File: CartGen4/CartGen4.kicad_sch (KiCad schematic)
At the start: 0 parts

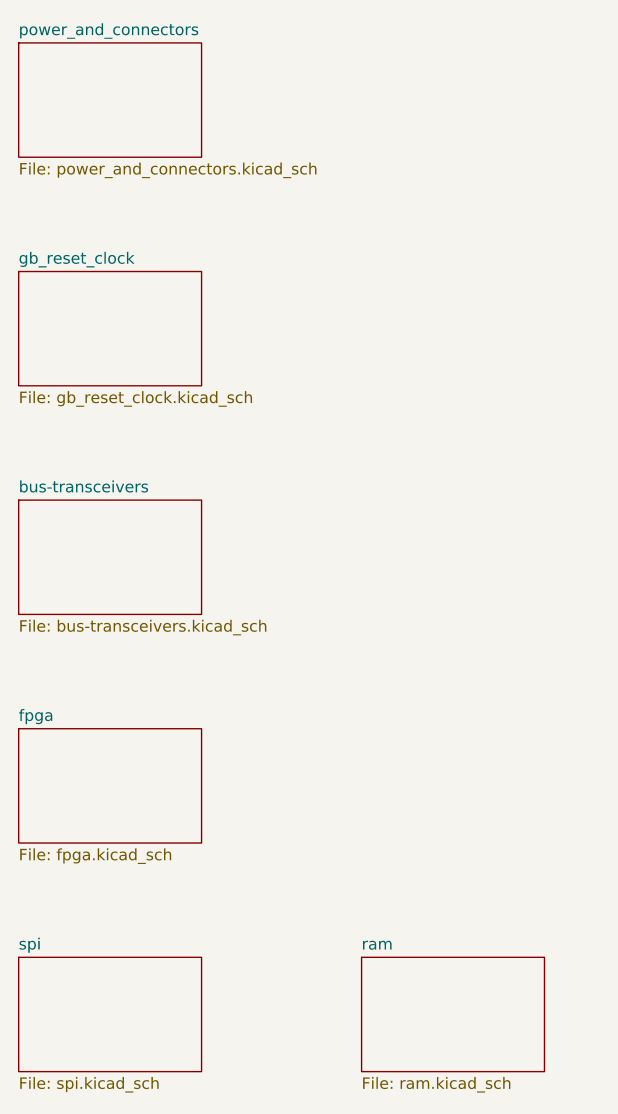
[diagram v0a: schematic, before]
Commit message: Made part of FPGA connections
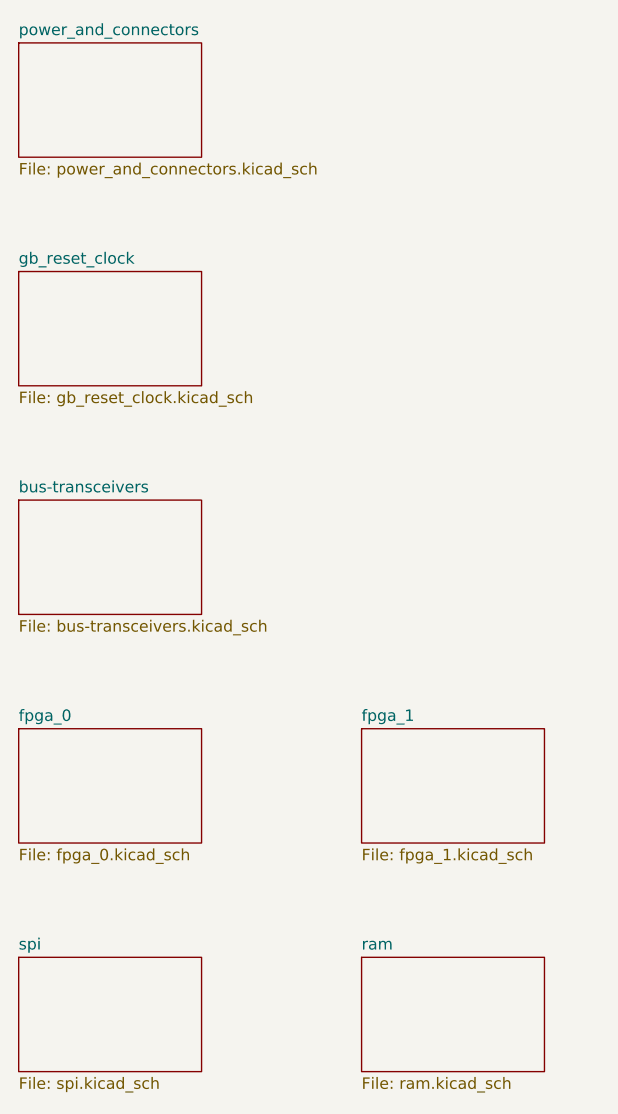
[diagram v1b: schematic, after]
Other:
- sheet fpga renamed fpga_0
- added sheet fpga_1 (fpga_1.kicad_sch)
- sheet fpga_0: file fpga.kicad_sch -> fpga_0.kicad_sch
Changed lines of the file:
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@@
     (stroke (width 0.1524) (type solid) (color 0 0 0 0))
     (fill (color 0 0 0 0.0000))
-    (property "Sheet name" "fpga" (id 0) (at 25.4 113.5884 0)
+    (property "Sheet name" "fpga_0" (id 0) (at 25.4 113.5884 0)
       (effects (font (size 1.27 1.27)) (justify left bottom))
     )
-    (property "Sheet file" "fpga.kicad_sch" (id 1) (at 25.4 127.5846 0)
+    (property "Sheet file" "fpga_0.kicad_sch" (id 1) (at 25.4 127.5846 0)
       (effects (font (size 1.27 1.27)) (justify left top))
     )
@@
     )
     (property "Sheet file" "spi.kicad_sch" (id 1) (at 25.4 152.9846 0)
+      (effects (font (size 1.27 1.27)) (justify left top))
+    )
+  )
+  (sheet (at 63.5 114.3) (size 20.32 12.7) (fields_autoplaced)
+    (stroke (width 0.1524) (type solid) (color 0 0 0 0))
+    (fill (color 0 0 0 0.0000))
+    (property "Sheet name" "fpga_1" (id 0) (at 63.5 113.5884 0)
+      (effects (font (size 1.27 1.27)) (justify left bottom))
+    )
+    (property "Sheet file" "fpga_1.kicad_sch" (id 1) (at 63.5 127.5846 0)
       (effects (font (size 1.27 1.27)) (justify left top))
     )
@@
     (path "/6fc5aafb-5a22-4bda-8f08-f38eb0e112cc" (page "6"))
     (path "/a842574a-62bd-4545-b3b1-b3137c6c2721" (page "7"))
+    (path "/c0de9d84-51e9-4175-bb13-3213096ac344" (page "8"))
   )
   (symbol_instances
@@
       (reference "#PWR?") (unit 1) (value "GND") (footprint "")
     )
+    (path "/89c162de-8374-4cb6-9c74-abac2a052a8d/11739f37-fca5-4f94-bf6e-f05776ff36fd"
+      (reference "#PWR?") (unit 1) (value "GND") (footprint "")
+    )
+    (path "/89c162de-8374-4cb6-9c74-abac2a052a8d/12a3c843-c8eb-48b3-8a2b-58f9ec7518d6"
+      (reference "#PWR?") (unit 1) (value "+3V3") (footprint "")
+    )
     (path "/67020394-371c-451d-9641-dd6c212cfc5e/139bed1b-d7ef-48f0-93a7-b2ee5c35ebdd"
       (reference "#PWR?") (unit 1) (value "+5V") (footprint "")
     )
+    (path "/89c162de-8374-4cb6-9c74-abac2a052a8d/142bd46e-5022-4e6c-9d6b-9e8fc9b8b5a2"
+      (reference "#PWR?") (unit 1) (value "GND") (footprint "")
+    )
     (path "/76bc839d-93e8-4c60-b95d-ac552335ae99/1b4e3723-e6cb-4b16-988b-c3305af91a5e"
       (reference "#PWR?") (unit 1) (value "GND") (footprint "")
@@
     (path "/67020394-371c-451d-9641-dd6c212cfc5e/1c391842-edf3-4ef2-9257-4d106ed1b380"
       (reference "#PWR?") (unit 1) (value "GND") (footprint "")
+    )
+    (path "/89c162de-8374-4cb6-9c74-abac2a052a8d/1d90c8fe-6680-4a2a-ae52-6871af96de94"
+      (reference "#PWR?") (unit 1) (value "GND") (footprint "")
+    )
+    (path "/89c162de-8374-4cb6-9c74-abac2a052a8d/1e8f1802-5e65-4a38-a899-cb4ea4774e61"
+      (reference "#PWR?") (unit 1) (value "+3V3") (footprint "")
+    )
+    (path "/89c162de-8374-4cb6-9c74-abac2a052a8d/225b4957-d158-4820-9542-5666ab3bb880"
+      (reference "#PWR?") (unit 1) (value "+3V3") (footprint "")
     )
     (path "/a842574a-62bd-4545-b3b1-b3137c6c2721/265d538c-9c43-43fe-861e-e8a64c296a5c"
@@
       (reference "#PWR?") (unit 1) (value "GND") (footprint "")
     )
+    (path "/89c162de-8374-4cb6-9c74-abac2a052a8d/3b61e718-d8b6-41c1-9a58-98ad21c68960"
+      (reference "#PWR?") (unit 1) (value "GND") (footprint "")
+    )
+    (path "/89c162de-8374-4cb6-9c74-abac2a052a8d/3e2d14df-4feb-41f5-8245-39c49558b752"
+      (reference "#PWR?") (unit 1) (value "+1V8") (footprint "")
+    )
+    (path "/89c162de-8374-4cb6-9c74-abac2a052a8d/4108126f-d227-4819-9c12-f364cd5bb76b"
+      (reference "#PWR?") (unit 1) (value "GND") (footprint "")
+    )
     (path "/a842574a-62bd-4545-b3b1-b3137c6c2721/4694efdb-3b6d-491b-8dbf-ec3b4909295d"
       (reference "#PWR?") (unit 1) (value "GND") (footprint "")
@@
       (reference "#PWR?") (unit 1) (value "+3.3V") (footprint "")
     )
+    (path "/89c162de-8374-4cb6-9c74-abac2a052a8d/6c3a4a37-01ca-4bdc-8d1b-7ba403960e15"
+      (reference "#PWR?") (unit 1) (value "+1V8") (footprint "")
+    )
     (path "/76bc839d-93e8-4c60-b95d-ac552335ae99/6ddeb701-c167-4f07-b69f-c3ad317df212"
       (reference "#PWR?") (unit 1) (value "+1V8") (footprint "")
@@
       (reference "#PWR?") (unit 1) (value "+3V3") (footprint "")
     )
+    (path "/89c162de-8374-4cb6-9c74-abac2a052a8d/81975237-87d0-4ccf-948f-3491e3cf30f9"
+      (reference "#PWR?") (unit 1) (value "GND") (footprint "")
+    )
+    (path "/89c162de-8374-4cb6-9c74-abac2a052a8d/87596f08-48d3-4fa9-8c80-41b1e93af53e"
+      (reference "#PWR?") (unit 1) (value "GND") (footprint "")
+    )
     (path "/a842574a-62bd-4545-b3b1-b3137c6c2721/97b2c2fb-5589-41f0-bcb4-c80098f1ce20"
       (reference "#PWR?") (unit 1) (value "+3V3") (footprint "")
@@
     (path "/a842574a-62bd-4545-b3b1-b3137c6c2721/ae1dd4cd-b33f-493a-adda-4871546ee7b9"
       (reference "#PWR?") (unit 1) (value "+3V3") (footprint "")
+    )
+    (path "/89c162de-8374-4cb6-9c74-abac2a052a8d/b0e086bb-5f08-4fa3-aa56-9752d059ec3a"
+      (reference "#PWR?") (unit 1) (value "GND") (footprint "")
+    )
+    (path "/89c162de-8374-4cb6-9c74-abac2a052a8d/b59a572b-45e4-4532-9f92-de20c7c8cb61"
+      (reference "#PWR?") (unit 1) (value "+1V2") (footprint "")
     )
     (path "/67020394-371c-451d-9641-dd6c212cfc5e/b9902037-5e38-4fae-b92f-82749be53d58"
@@
       (reference "#PWR?") (unit 1) (value "GND") (footprint "")
     )
+    (path "/89c162de-8374-4cb6-9c74-abac2a052a8d/ee7273cb-29f0-431b-9564-1484e7ff57e4"
+      (reference "#PWR?") (unit 1) (value "GND") (footprint "")
+    )
+    (path "/89c162de-8374-4cb6-9c74-abac2a052a8d/fe86db9d-024d-4c1b-ad00-b68d647fb39f"
+      (reference "#PWR?") (unit 1) (value "GND") (footprint "")
+    )
     (path "/4ef07d45-f940-4cb6-bb96-2ddec13fd099/1b8d5810-67b5-41f5-a4e9-e6c2cc9fec50"
       (reference "A1") (unit 1) (value "GBC_Cart") (footprint "Boards:GBC_Cart")
@@
       (reference "C29") (unit 1) (value "100n") (footprint "")
     )
+    (path "/89c162de-8374-4cb6-9c74-abac2a052a8d/078184b6-0da5-41f5-afda-98550db77527"
+      (reference "C?") (unit 1) (value "100n") (footprint "")
+    )
     (path "/a842574a-62bd-4545-b3b1-b3137c6c2721/373bb0b0-a4d2-4f2a-8738-01c5270f27b1"
       (reference "C?") (unit 1) (value "100n") (footprint "")
     )
+    (path "/89c162de-8374-4cb6-9c74-abac2a052a8d/50fc1c29-d361-43dd-a0fb-8c9fe60d0659"
+      (reference "C?") (unit 1) (value "100n") (footprint "")
+    )
     (path "/a842574a-62bd-4545-b3b1-b3137c6c2721/558dcd05-2eea-4117-a2da-11884722a4cd"
       (reference "C?") (unit 1) (value "100n") (footprint "")
     )
+    (path "/89c162de-8374-4cb6-9c74-abac2a052a8d/6d80228b-879b-491e-a2ae-3b9511b8eac5"
+      (reference "C?") (unit 1) (value "100n") (footprint "")
+    )
+    (path "/89c162de-8374-4cb6-9c74-abac2a052a8d/9448eb54-7699-47c3-b179-3c5f89510ba3"
+      (reference "C?") (unit 1) (value "100n") (footprint "")
+    )
     (path "/a842574a-62bd-4545-b3b1-b3137c6c2721/98a36b99-198d-4837-aeab-8049fd52403d"
       (reference "C?") (unit 1) (value "100n") (footprint "")
     )
+    (path "/89c162de-8374-4cb6-9c74-abac2a052a8d/9aa78323-e08d-422c-acc3-2fe65a0e59de"
+      (reference "C?") (unit 1) (value "100n") (footprint "")
+    )
+    (path "/89c162de-8374-4cb6-9c74-abac2a052a8d/b8ad21cd-e125-4ef3-a62b-24505dde5db2"
+      (reference "C?") (unit 1) (value "100n") (footprint "")
+    )
+    (path "/89c162de-8374-4cb6-9c74-abac2a052a8d/b9fb30eb-ec3d-4232-bd9b-fa6623a16022"
+      (reference "C?") (unit 1) (value "100n") (footprint "")
+    )
     (path "/76bc839d-93e8-4c60-b95d-ac552335ae99/d65d6728-2380-456a-a9d1-baa122edbe74"
+      (reference "C?") (unit 1) (value "100n") (footprint "")
+    )
+    (path "/89c162de-8374-4cb6-9c74-abac2a052a8d/f1625e4c-36b3-49f5-884d-ead49f4fc100"
+      (reference "C?") (unit 1) (value "100n") (footprint "")
+    )
+    (path "/89c162de-8374-4cb6-9c74-abac2a052a8d/f73fb9c5-5bb1-4964-8d44-b0ed2a74fe22"
+      (reference "C?") (unit 1) (value "100n") (footprint "")
+    )
+    (path "/89c162de-8374-4cb6-9c74-abac2a052a8d/fc7e2b43-d24b-474c-a580-7787c8c83ac7"
       (reference "C?") (unit 1) (value "100n") (footprint "")
     )
@@
       (reference "R?") (unit 1) (value "1K") (footprint "")
     )
+    (path "/89c162de-8374-4cb6-9c74-abac2a052a8d/7654073d-1914-4ee1-8f36-646833a88e23"
+      (reference "R?") (unit 1) (value "15K") (footprint "")
+    )
     (path "/a842574a-62bd-4545-b3b1-b3137c6c2721/7a4dfc61-c8b1-4854-ae82-5d7fef6573a4"
       (reference "R?") (unit 1) (value "15K") (footprint "")
@@
       (reference "U?") (unit 1) (value "NXS0104BQX") (footprint "")
     )
-    (path "/89c162de-8374-4cb6-9c74-abac2a052a8d/1765047d-477d-4e9e-a14b-c311772de8ac"
+    (path "/c0de9d84-51e9-4175-bb13-3213096ac344/b22717d6-2844-4c78-947b-a0405ed8333f"
       (reference "U?") (unit 2) (value "LFXP2-8E-5MN132C") (footprint "")
     )
@@
       (reference "U?") (unit 3) (value "LFXP2-8E-5MN132C") (footprint "")
     )
-    (path "/89c162de-8374-4cb6-9c74-abac2a052a8d/c39ad1a9-2c59-481d-9cf3-32a127a43b1d"
+    (path "/c0de9d84-51e9-4175-bb13-3213096ac344/13daf24f-86a4-4ec2-8fe2-9b00696ea8e9"
       (reference "U?") (unit 4) (value "LFXP2-8E-5MN132C") (footprint "")
     )
-    (path "/89c162de-8374-4cb6-9c74-abac2a052a8d/03031b1d-3503-4fbb-bb1d-d0daee267daa"
+    (path "/c0de9d84-51e9-4175-bb13-3213096ac344/d30a5470-ed75-4279-b024-60a3530e023b"
       (reference "U?") (unit 5) (value "LFXP2-8E-5MN132C") (footprint "")
     )
-    (path "/89c162de-8374-4cb6-9c74-abac2a052a8d/c0ae4ece-7462-465e-9c01-02b01c36e260"
+    (path "/c0de9d84-51e9-4175-bb13-3213096ac344/e312b235-fa9d-4146-a238-9cc6d5599ffa"
       (reference "U?") (unit 6) (value "LFXP2-8E-5MN132C") (footprint "")
     )
-    (path "/89c162de-8374-4cb6-9c74-abac2a052a8d/f190f8af-9d18-4cca-84ff-7cbb88c4fd8f"
+    (path "/c0de9d84-51e9-4175-bb13-3213096ac344/f6ea60e3-f584-4ae9-be4b-1a741cd1f8ac"
       (reference "U?") (unit 7) (value "LFXP2-8E-5MN132C") (footprint "")
     )

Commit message: Added copyright
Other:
- company: (none) -> © Elijah Almeida Coimbra
- title: (none) -> Root sheet
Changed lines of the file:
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@@
 (kicad_sch (version 20211123) (generator eeschema)
   (paper "A4")
+  (title_block
+    (title "Root sheet")
+    (company "© Elijah Almeida Coimbra")
+  )
   (sheet (at 25.4 38.1) (size 20.32 12.7) (fields_autoplaced)
     (stroke (width 0.1524) (type solid) (color 0 0 0 0))
